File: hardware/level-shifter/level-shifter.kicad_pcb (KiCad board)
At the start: 2 copper layers, 61.3 x 54.1 mm, 28 parts, among them J1 Conn_01x10_Socket, J2 Conn_01x10_Socket, J3 Conn_01x10_Socket, J4 Conn_01x10_Socket, J5 Conn_01x10_Pin, J6 Conn_01x10_Pin, J7 Conn_01x10_Pin, J8 Conn_01x10_Pin

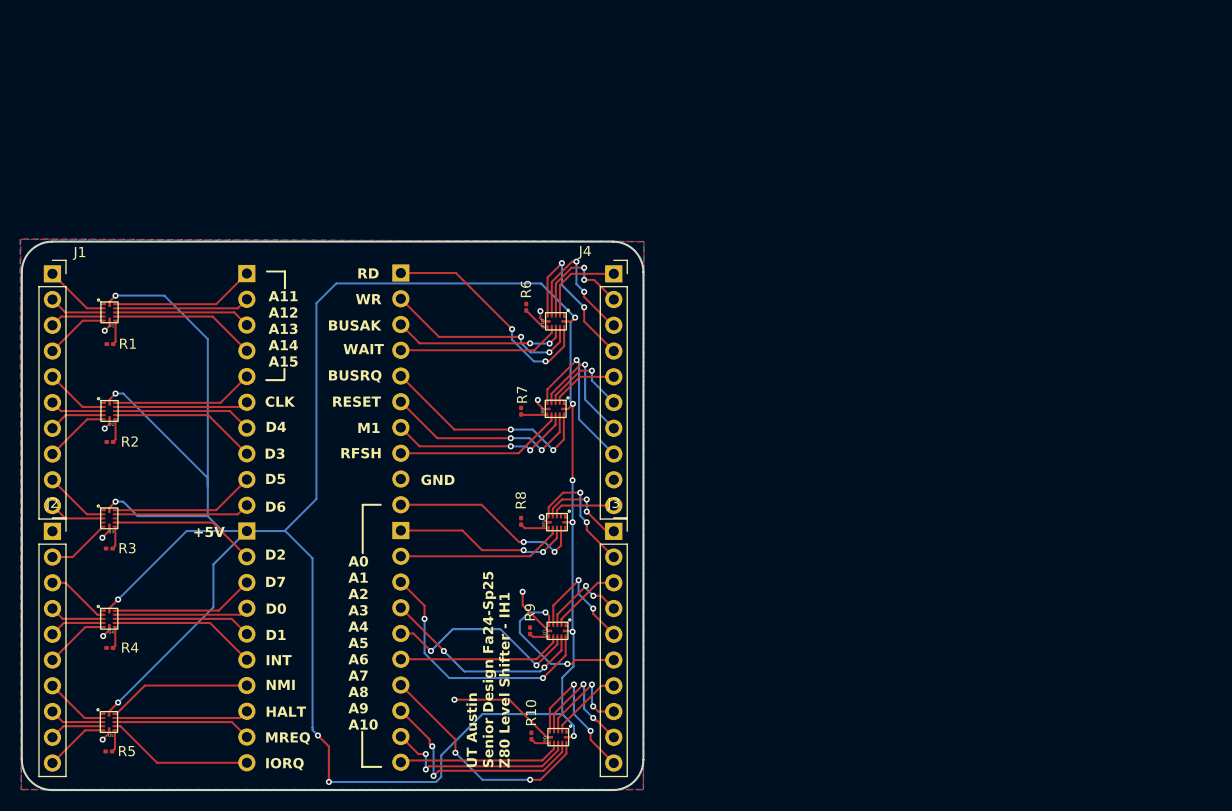
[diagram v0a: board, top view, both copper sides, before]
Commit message: level shifter redo
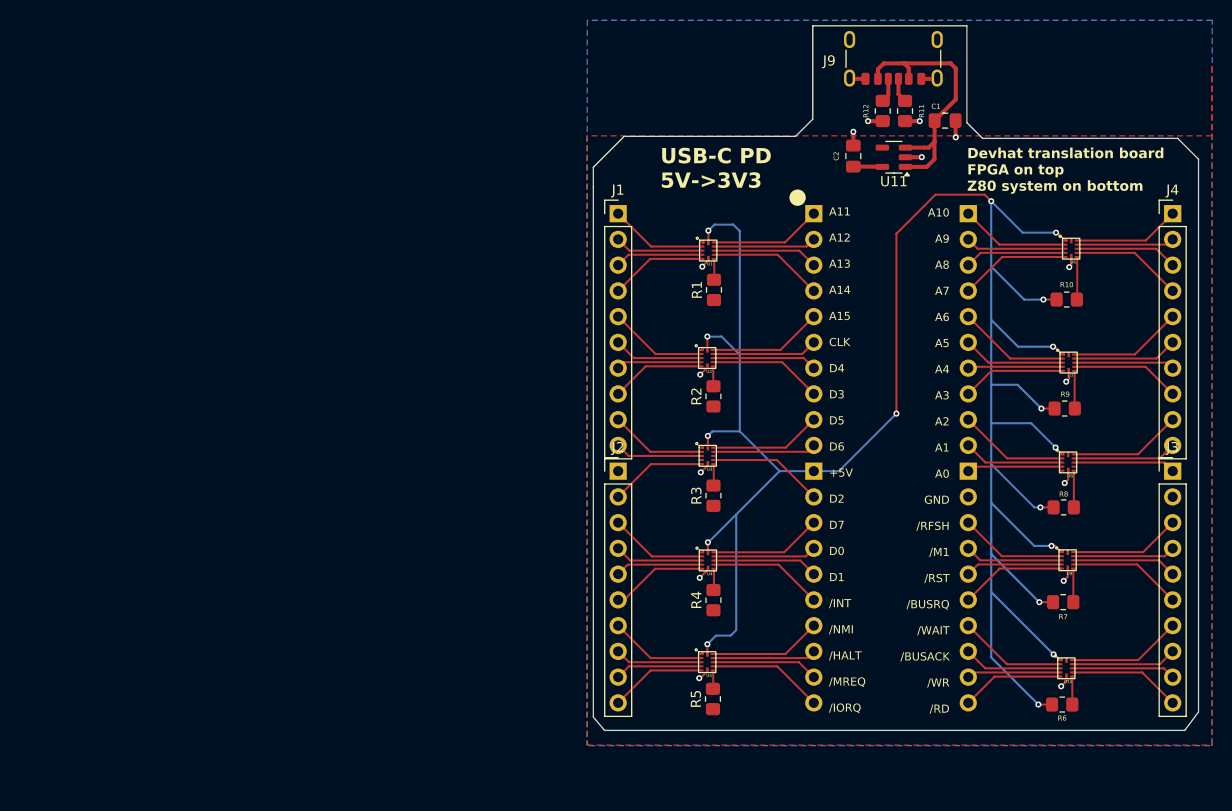
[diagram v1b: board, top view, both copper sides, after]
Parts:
- added C1: 10u, Capacitor_SMD:C_0805_2012Metric_Pad1.18x1.45mm_HandSolder, F.Cu at (152.9, 56.9)
- added C2: 10u, Capacitor_SMD:C_0805_2012Metric_Pad1.18x1.45mm_HandSolder, F.Cu at (143.9, 60.4)
- added J9: USB_C_Receptacle_PowerOnly_6P, Connector_USB:USB_C_Receptacle_GCT_USB4125-xx-x_6P_TopMnt_Horizontal, F.Cu at (147.8, 49.7)
- added R11: 5k1, Resistor_SMD:R_0805_2012Metric_Pad1.20x1.40mm_HandSolder, F.Cu at (149.0, 56.0)
- added R12: 5k1, Resistor_SMD:R_0805_2012Metric_Pad1.20x1.40mm_HandSolder, F.Cu at (146.8, 56.0)
- added U11: TLV75533PDBV, Package_TO_SOT_SMD:SOT-23-5, F.Cu at (147.9, 60.5)
- J1, J2, J3, J4: footprint Connector_PinSocket_2.54mm:PinSocket_1x10_P2.54mm_Vertical -> Connector_PinHeader_2.54mm:PinHeader_1x10_P2.54mm_Vertical
- R1, R10, R2, R3, R4, R5, R6, R7, R8, R9: footprint Resistor_SMD:R_0201_0603Metric -> Resistor_SMD:R_0805_2012Metric_Pad1.20x1.40mm_HandSolder
- moved R10 68.1 mm to (164.9, 74.5), turned to 0 degrees
- moved R6 65.8 mm to (164.5, 114.5), turned to 0 degrees
- moved U6 63.1 mm to (165.6, 70.9), turned to 0 degrees
- moved U4 61.0 mm to (129.7, 101.7)
- moved U1 61.0 mm to (129.8, 71.1)
- moved U3 60.9 mm to (129.7, 91.3)
- moved U5 60.9 mm to (129.7, 111.7)
- moved U2 60.9 mm to (129.7, 81.7)
- moved R3 59.8 mm to (130.1, 93.9), turned to 90 degrees
- moved R5 59.8 mm to (130.1, 114.0), turned to 90 degrees
- moved R1 59.8 mm to (130.2, 73.6), turned to 90 degrees
- moved R4 59.7 mm to (130.1, 104.2), turned to 90 degrees
- moved R2 59.7 mm to (130.1, 84.1), turned to 90 degrees
- moved U10 57.6 mm to (165.1, 112.3), turned to 0 degrees
- moved R9 57.1 mm to (164.8, 85.3), turned to 0 degrees
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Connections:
- J2 pad 1: +3V3 -> unconnected-(J2-Pin_1-Pad1)
- J3 pad 1: A1_FPGA -> A0_FPGA
- J3 pad 10: A10_FPGA -> RD_FPGA
- J3 pad 2: A2_FPGA -> unconnected-(J3-Pin_2-Pad2)
- J3 pad 3: A3_FPGA -> RFSH_FPGA
- J3 pad 4: A4_FPGA -> M1_FPGA
- J3 pad 5: A5_FPGA -> RESET_FPGA
- J3 pad 6: A6_FPGA -> BUSRQ_FPGA
- J3 pad 7: A7_FPGA -> WAIT_FPGA
- J3 pad 8: A8_FPGA -> BUSAK_FPGA
- J3 pad 9: A9_FPGA -> WR_FPGA
- J4 pad 1: RD_FPGA -> A10_FPGA
- J4 pad 10: A0_FPGA -> A1_FPGA
- J4 pad 2: WR_FPGA -> A9_FPGA
- J4 pad 3: BUSAK_FPGA -> A8_FPGA
- J4 pad 4: WAIT_FPGA -> A7_FPGA
- J4 pad 5: BUSRQ_FPGA -> A6_FPGA
- J4 pad 6: RESET_FPGA -> A5_FPGA
- J4 pad 7: M1_FPGA -> A4_FPGA
- J4 pad 8: RFSH_FPGA -> A3_FPGA
- J4 pad 9: unconnected-(J4-Pin_9-Pad9) -> A2_FPGA
- J7 pad 1: RD_5V -> A10_5V
- J7 pad 10: A0_5V -> A1_5V
- J7 pad 2: WR_5V -> A9_5V
- J7 pad 3: BUSAK_5V -> A8_5V
- J7 pad 4: WAIT_5V -> A7_5V
- J7 pad 5: BUSRQ_5V -> A6_5V
- J7 pad 6: RESET_5V -> A5_5V
- J7 pad 7: M1_5V -> A4_5V
- J7 pad 8: RFSH_5V -> A3_5V
- J7 pad 9: GND -> A2_5V
- J8 pad 1: A1_5V -> A0_5V
- J8 pad 10: A10_5V -> RD_5V
- J8 pad 2: A2_5V -> GND
- J8 pad 3: A3_5V -> RFSH_5V
- J8 pad 4: A4_5V -> M1_5V
- J8 pad 5: A5_5V -> RESET_5V
- J8 pad 6: A6_5V -> BUSRQ_5V
- J8 pad 7: A7_5V -> WAIT_5V
- J8 pad 8: A8_5V -> BUSAK_5V
- J8 pad 9: A9_5V -> WR_5V
- R10 pad 1: +3V3 -> +5V
- R6 pad 1: +3V3 -> +5V
- R7 pad 1: +3V3 -> +5V
- R8 pad 1: +3V3 -> +5V
- R9 pad 1: +3V3 -> +5V
- U10 pad 1: +3V3 -> +5V
- U10 pad 10: WR_5V -> BUSAK_FPGA
- U10 pad 11: RD_5V -> WAIT_FPGA
- U10 pad 12: +5V -> +3V3
- U10 pad 2: RD_FPGA -> WAIT_5V
- U10 pad 3: WR_FPGA -> BUSAK_5V
- U10 pad 4: BUSAK_FPGA -> WR_5V
- U10 pad 5: WAIT_FPGA -> RD_5V
- U10 pad 8: WAIT_5V -> RD_FPGA
- U10 pad 9: BUSAK_5V -> WR_FPGA
- U6 pad 1: +3V3 -> +5V
- U6 pad 10: A8_5V -> A9_FPGA
- U6 pad 11: A7_5V -> A10_FPGA
- U6 pad 12: +5V -> +3V3
- U6 pad 2: A7_FPGA -> A10_5V
- U6 pad 3: A8_FPGA -> A9_5V
- U6 pad 4: A9_FPGA -> A8_5V
- U6 pad 5: A10_FPGA -> A7_5V
- U6 pad 8: A10_5V -> A7_FPGA
- U6 pad 9: A9_5V -> A8_FPGA
- U7 pad 1: +3V3 -> +5V
- U7 pad 10: A4_5V -> A5_FPGA
- U7 pad 11: A3_5V -> A6_FPGA
- U7 pad 12: +5V -> +3V3
- U7 pad 2: A3_FPGA -> A6_5V
- U7 pad 3: A4_FPGA -> A5_5V
- U7 pad 4: A5_FPGA -> A4_5V
- U7 pad 5: A6_FPGA -> A3_5V
- U7 pad 8: A6_5V -> A3_FPGA
- U7 pad 9: A5_5V -> A4_FPGA
- U8 pad 1: +3V3 -> +5V
- U8 pad 10: A0_5V -> A1_FPGA
- U8 pad 11: unconnected-(U8-B1-Pad11) -> A2_FPGA
- U8 pad 12: +5V -> +3V3
- U8 pad 2: unconnected-(U8-A1-Pad2) -> A2_5V
- U8 pad 3: A0_FPGA -> A1_5V
- U8 pad 4: A1_FPGA -> A0_5V
- U8 pad 5: A2_FPGA -> unconnected-(U8-A4-Pad5)
- U8 pad 8: A2_5V -> unconnected-(U8-B4-Pad8)
- U8 pad 9: A1_5V -> A0_FPGA
- U9 pad 1: +3V3 -> +5V
- U9 pad 10: RESET_5V -> M1_FPGA
- U9 pad 11: BUSRQ_5V -> RFSH_FPGA
- U9 pad 12: +5V -> +3V3
- U9 pad 2: BUSRQ_FPGA -> RFSH_5V
- U9 pad 3: RESET_FPGA -> M1_5V
- U9 pad 4: M1_FPGA -> RESET_5V
- U9 pad 5: RFSH_FPGA -> BUSRQ_5V
- U9 pad 8: RFSH_5V -> BUSRQ_FPGA
- U9 pad 9: M1_5V -> RESET_FPGA
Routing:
- net Net-(U11-EN): track 0.00 -> 26.9 mm
- net +5V: track 257.8 -> 239.1 mm, vias 13 -> 17
- net A3_5V: track 25.7 -> 10.2 mm, vias 2 -> 0
- net RD_5V: track 22.8 -> 10.1 mm, vias 2 -> 0
- net A8_5V: track 22.3 -> 10.0 mm, vias 2 -> 0
- net A7_5V: track 23.1 -> 10.9 mm, vias 2 -> 0
- net BUSRQ_5V: track 22.0 -> 10.5 mm, vias 2 -> 0
- net A4_5V: track 20.7 -> 9.33 mm, vias 2 -> 0
- net WR_5V: track 20.1 -> 9.24 mm, vias 2 -> 0
- net RESET_5V: track 20.1 -> 9.57 mm, vias 2 -> 0
- net A0_5V: track 19.7 -> 9.41 mm, vias 2 -> 0
- net A5_5V: track 20.1 -> 10.1 mm, vias 2 -> 0
- net A9_5V: track 19.2 -> 9.91 mm, vias 2 -> 0
- net M1_5V: track 18.2 -> 9.66 mm, vias 2 -> 0
- net A1_5V: track 17.8 -> 9.92 mm, vias 2 -> 0
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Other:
- board size 61.3 x 54.1 mm -> 59.7 x 69.5 mm
- board text added: "A10 A9 A8 A7 A6 A5 A4 A3 A2 A1 A0 GND /RFSH /M1 /RST /BUSRQ /WAIT /BUSACK /WR /RD"
- board text added: "A11 A12 A13 A14 A15 CLK D4 D3 D5 D6 +5V D2 D7 D0 D1 /INT /NMI /HALT /MREQ /IORQ"
- board text added: "Devhat translation board FPGA on top Z80 system on bottom"
- board text added: "USB-C PD 5V->3V3"
- board text removed: "+5V"
- board text removed: "0.6{dblquote} wide (15.24mm) 2.0{dblquote} height (50.8mm)"
- board text removed: "A0 A1 A2 A3 A4 A5 A6 A7 A8 A9 A10"
- board text removed: "A11 A12 A13 A14 A15"
- board text removed: "BUSAK"
- board text removed: "BUSRQ"
- board text removed: "CLK"
- board text removed: "D0"
- board text removed: "D1"
- board text removed: "D2"
- board text removed: "D3"
- board text removed: "D4"
- board text removed: "D5"
- board text removed: "D6"
- board text removed: "D7"
- board text removed: "GND"
- board text removed: "HALT"
- board text removed: "INT"
- board text removed: "IORQ"
- board text removed: "M1"
- board text removed: "MREQ"
- board text removed: "NMI"
- board text removed: "RD"
- board text removed: "RESET"
- board text removed: "RFSH"
- board text removed: "UT Austin Senior Design Fa24-Sp25 Z80 Level Shifter - IH1"
- board text removed: "WAIT"
- board text removed: "WR"
